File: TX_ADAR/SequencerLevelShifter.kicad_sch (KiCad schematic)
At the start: 16 parts, among them SW4 SW_SPDT, SW6 SW_SPST, SW7 SW_SPST, U15 TXB0101DBV, U16 TXB0101DBV, U17 TXB0101DBV, U18 TXB0101DBV

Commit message: Fixed more issues
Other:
- note removed: "For reset pins, have them reset every time power is turned on?"
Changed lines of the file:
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@@
 	(generator_version "10.0")
 	(paper "A4")
-	(text "For reset pins, have them reset \nevery time power is turned on?"
-		(exclude_from_sim no)
-		(at 167.64 106.426 0)
-		(effects
-			(font
-				(size 2.54 2.54)
-			)
-		)
-	)
 	(text "Level Shifters\n3V3 -> 1V8"
 		(exclude_from_sim no)

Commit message: Finished up adding footprints. Removed unnecessary switches for the TxRST and MRST
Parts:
- removed SW6, SW7: SW_SPST, symbol Switch:SW_SPST
- C29, C30, C31, C38, C39, C40, C41, C42: footprint (none) -> Capacitor_SMD:C_0603_1608Metric_Pad1.08x0.95mm_HandSolder
- R4: footprint (none) -> Resistor_SMD:R_0603_1608Metric_Pad0.98x0.95mm_HandSolder
- SW4: footprint (none) -> 100SP1T1B4M2QE:SW_100SP1T1B4M2QE
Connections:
- net MRST Out: now also U18.4 (B)
- net TxRST Out: now also U16.4 (B)
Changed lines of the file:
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@@
 	(wire
 		(pts
-			(xy 237.49 82.55) (xy 237.49 86.36)
+			(xy 237.49 59.69) (xy 237.49 76.2)
 		)
 		(stroke
@@
 	(wire
 		(pts
-			(xy 162.56 82.55) (xy 162.56 86.36)
+			(xy 189.23 69.85) (xy 226.06 69.85)
 		)
 		(stroke
@@
 	(wire
 		(pts
-			(xy 189.23 69.85) (xy 226.06 69.85)
+			(xy 236.22 59.69) (xy 237.49 59.69)
 		)
 		(stroke
@@
 	(wire
 		(pts
-			(xy 236.22 59.69) (xy 237.49 59.69)
+			(xy 161.29 29.21) (xy 186.69 29.21)
+		)
+		(stroke
+			(width 0.254)
+			(type default)
+			(color 46 82 255 1)
+		)
+	)
+	(wire
+		(pts
+			(xy 209.55 45.72) (xy 198.12 45.72)
+		)
+		(stroke
+			(width 0.254)
+			(type default)
+			(color 255 180 68 1)
+		)
+	)
+	(wire
+		(pts
+			(xy 177.8 73.66) (xy 177.8 59.69)
 		)
 		(stroke
@@
 	(wire
 		(pts
-			(xy 161.29 29.21) (xy 186.69 29.21)
+			(xy 186.69 29.21) (xy 198.12 29.21)
 		)
 		(stroke
@@
 	(wire
 		(pts
-			(xy 209.55 45.72) (xy 198.12 45.72)
+			(xy 172.72 45.72) (xy 161.29 45.72)
 		)
 		(stroke
@@
 	(wire
 		(pts
-			(xy 177.8 73.66) (xy 177.8 59.69)
+			(xy 172.72 26.67) (xy 191.77 26.67)
+		)
+		(stroke
+			(width 0.254)
+			(type default)
+			(color 255 180 68 1)
+		)
+	)
+	(wire
+		(pts
+			(xy 138.43 59.69) (xy 138.43 74.93)
 		)
 		(stroke
@@
 	(wire
 		(pts
-			(xy 186.69 29.21) (xy 198.12 29.21)
+			(xy 161.29 41.91) (xy 161.29 45.72)
 		)
 		(stroke
@@
 	(wire
 		(pts
-			(xy 172.72 45.72) (xy 161.29 45.72)
+			(xy 35.56 36.83) (xy 39.37 36.83)
+		)
+		(stroke
+			(width 0)
+			(type default)
+		)
+	)
+	(wire
+		(pts
+			(xy 161.29 29.21) (xy 161.29 34.29)
+		)
+		(stroke
+			(width 0.254)
+			(type default)
+			(color 46 82 255 1)
+		)
+	)
+	(wire
+		(pts
+			(xy 111.76 24.13) (xy 111.76 49.53)
 		)
 		(stroke
@@
 	(wire
 		(pts
-			(xy 237.49 59.69) (xy 237.49 72.39)
-		)
-		(stroke
-			(width 0)
-			(type default)
-		)
-	)
-	(wire
-		(pts
-			(xy 172.72 26.67) (xy 191.77 26.67)
-		)
-		(stroke
-			(width 0.254)
-			(type default)
-			(color 255 180 68 1)
-		)
-	)
-	(wire
-		(pts
-			(xy 138.43 59.69) (xy 138.43 74.93)
-		)
-		(stroke
-			(width 0)
-			(type default)
-		)
-	)
-	(wire
-		(pts
-			(xy 161.29 41.91) (xy 161.29 45.72)
-		)
-		(stroke
-			(width 0.254)
-			(type default)
-			(color 46 82 255 1)
-		)
-	)
-	(wire
-		(pts
-			(xy 35.56 36.83) (xy 39.37 36.83)
-		)
-		(stroke
-			(width 0)
-			(type default)
-		)
-	)
-	(wire
-		(pts
-			(xy 161.29 29.21) (xy 161.29 34.29)
-		)
-		(stroke
-			(width 0.254)
-			(type default)
-			(color 46 82 255 1)
-		)
-	)
-	(wire
-		(pts
-			(xy 111.76 24.13) (xy 111.76 49.53)
-		)
-		(stroke
-			(width 0.254)
-			(type default)
-			(color 255 180 68 1)
-		)
-	)
-	(wire
-		(pts
-			(xy 162.56 59.69) (xy 162.56 72.39)
+			(xy 162.56 59.69) (xy 162.56 76.2)
 		)
 		(stroke
@@
 	(hierarchical_label "TxRST Out"
 		(shape output)
-		(at 162.56 86.36 270)
+		(at 162.56 76.2 270)
 		(effects
 			(font
@@
 	(hierarchical_label "MRST Out"
 		(shape output)
-		(at 237.49 86.36 270)
+		(at 237.49 76.2 270)
 		(effects
 			(font
@@
 			)
 		)
-		(property "Footprint" ""
+		(property "Footprint" "Capacitor_SMD:C_0603_1608Metric_Pad1.08x0.95mm_HandSolder"
 			(at 86.0552 41.91 0)
 			(hide yes)
@@
 			)
 		)
-		(property "Footprint" ""
+		(property "Footprint" "Capacitor_SMD:C_0603_1608Metric_Pad1.08x0.95mm_HandSolder"
 			(at 74.6252 41.91 0)
 			(hide yes)
@@
 			)
 		)
-		(property "Footprint" ""
+		(property "Footprint" "100SP1T1B4M2QE:SW_100SP1T1B4M2QE"
 			(at 30.48 39.37 0)
 			(hide yes)
@@
 			)
 		)
-		(property "Footprint" ""
+		(property "Footprint" "Capacitor_SMD:C_0603_1608Metric_Pad1.08x0.95mm_HandSolder"
 			(at 210.5152 41.91 0)
 			(hide yes)
@@
 				(path "/5bb7bcfe-c6dc-48dd-b109-2cc47fd52212/81ed6aba-4ce9-46a8-9f2a-cfb086f29798"
 					(reference "C42")
-					(unit 1)
-				)
-			)
-		)
-	)
-	(symbol
-		(lib_id "Switch:SW_SPST")
-		(at 237.49 77.47 90)
-		(unit 1)
-		(body_style 1)
-		(exclude_from_sim no)
-		(in_bom yes)
-		(on_board yes)
-		(in_pos_files yes)
-		(dnp no)
-		(fields_autoplaced yes)
-		(property "Reference" "SW7"
-			(at 238.76 76.1999 90)
-			(show_name no)
-			(do_not_autoplace no)
-			(effects
-				(font
-					(size 1.27 1.27)
-				)
-				(justify right)
-			)
-		)
-		(property "Value" "SW_SPST"
-			(at 238.76 78.7399 90)
-			(hide yes)
-			(show_name no)
-			(do_not_autoplace no)
-			(effects
-				(font
-					(size 1.27 1.27)
-				)
-				(justify right)
-			)
-		)
-		(property "Footprint" ""
-			(at 237.49 77.47 0)
-			(hide yes)
-			(show_name no)
-			(do_not_autoplace no)
-			(effects
-				(font
-					(size 1.27 1.27)
-				)
-			)
-		)
-		(property "Datasheet" ""
-			(at 237.49 77.47 0)
-			(hide yes)
-			(show_name no)
-			(do_not_autoplace no)
-			(effects
-				(font
-					(size 1.27 1.27)
-				)
-			)
-		)
-		(property "Description" "Single Pole Single Throw (SPST) switch"
-			(at 237.49 77.47 0)
-			(hide yes)
-			(show_name no)
-			(do_not_autoplace no)
-			(effects
-				(font
-					(size 1.27 1.27)
-				)
-			)
-		)
-		(pin "1"
-		)
-		(pin "2"
-		)
-		(instances
-			(project "TX_ADAR"
-				(path "/5bb7bcfe-c6dc-48dd-b109-2cc47fd52212/81ed6aba-4ce9-46a8-9f2a-cfb086f29798"
-					(reference "SW7")
 					(unit 1)
 				)
@@
 			)
 		)
-		(property "Footprint" ""
+		(property "Footprint" "Capacitor_SMD:C_0603_1608Metric_Pad1.08x0.95mm_HandSolder"
 			(at 134.3152 41.91 0)
 			(hide yes)
@@
 			)
 		)
-		(property "Footprint" ""
+		(property "Footprint" "Capacitor_SMD:C_0603_1608Metric_Pad1.08x0.95mm_HandSolder"
 			(at 122.8852 41.91 0)
 			(hide yes)
@@
 			)
 		)
-		(property "Footprint" ""
+		(property "Footprint" "Capacitor_SMD:C_0603_1608Metric_Pad1.08x0.95mm_HandSolder"
 			(at 199.0852 41.91 0)
 			(hide yes)
@@
 			)
 		)
-		(property "Footprint" ""
+		(property "Footprint" "Capacitor_SMD:C_0603_1608Metric_Pad1.08x0.95mm_HandSolder"
 			(at 162.2552 41.91 0)
 			(hide yes)
@@
 				(path "/5bb7bcfe-c6dc-48dd-b109-2cc47fd52212/81ed6aba-4ce9-46a8-9f2a-cfb086f29798"
 					(reference "C39")
-					(unit 1)
-				)
-			)
-		)
-	)
-	(symbol
-		(lib_id "Switch:SW_SPST")
-		(at 162.56 77.47 90)
-		(unit 1)
-		(body_style 1)
-		(exclude_from_sim no)
-		(in_bom yes)
-		(on_board yes)
-		(in_pos_files yes)
-		(dnp no)
-		(fields_autoplaced yes)
-		(property "Reference" "SW6"
-			(at 163.83 76.1999 90)
-			(show_name no)
-			(do_not_autoplace no)
-			(effects
-				(font
-					(size 1.27 1.27)
-				)
-				(justify right)
-			)
-		)
-		(property "Value" "SW_SPST"
-			(at 163.83 78.7399 90)
-			(hide yes)
-			(show_name no)
-			(do_not_autoplace no)
-			(effects
-				(font
-					(size 1.27 1.27)
-				)
-				(justify right)
-			)
-		)
-		(property "Footprint" ""
-			(at 162.56 77.47 0)
-			(hide yes)
-			(show_name no)
-			(do_not_autoplace no)
-			(effects
-				(font
-					(size 1.27 1.27)
-				)
-			)
-		)
-		(property "Datasheet" ""
-			(at 162.56 77.47 0)
-			(hide yes)
-			(show_name no)
-			(do_not_autoplace no)
-			(effects
-				(font
-					(size 1.27 1.27)
-				)
-			)
-		)
-		(property "Description" "Single Pole Single Throw (SPST) switch"
-			(at 162.56 77.47 0)
-			(hide yes)
-			(show_name no)
-			(do_not_autoplace no)
-			(effects
-				(font
-					(size 1.27 1.27)
-				)
-			)
-		)
-		(pin "1"
-		)
-		(pin "2"
-		)
-		(instances
-			(project "TX_ADAR"
-				(path "/5bb7bcfe-c6dc-48dd-b109-2cc47fd52212/81ed6aba-4ce9-46a8-9f2a-cfb086f29798"
-					(reference "SW6")
 					(unit 1)
 				)
@@
 			)
 		)
-		(property "Footprint" ""
+		(property "Footprint" "Capacitor_SMD:C_0603_1608Metric_Pad1.08x0.95mm_HandSolder"
 			(at 173.6852 41.91 0)
 			(hide yes)
@@
 			)
 		)
-		(property "Footprint" ""
+		(property "Footprint" "Resistor_SMD:R_0603_1608Metric_Pad0.98x0.95mm_HandSolder"
 			(at 39.37 31.75 0)
 			(hide yes)

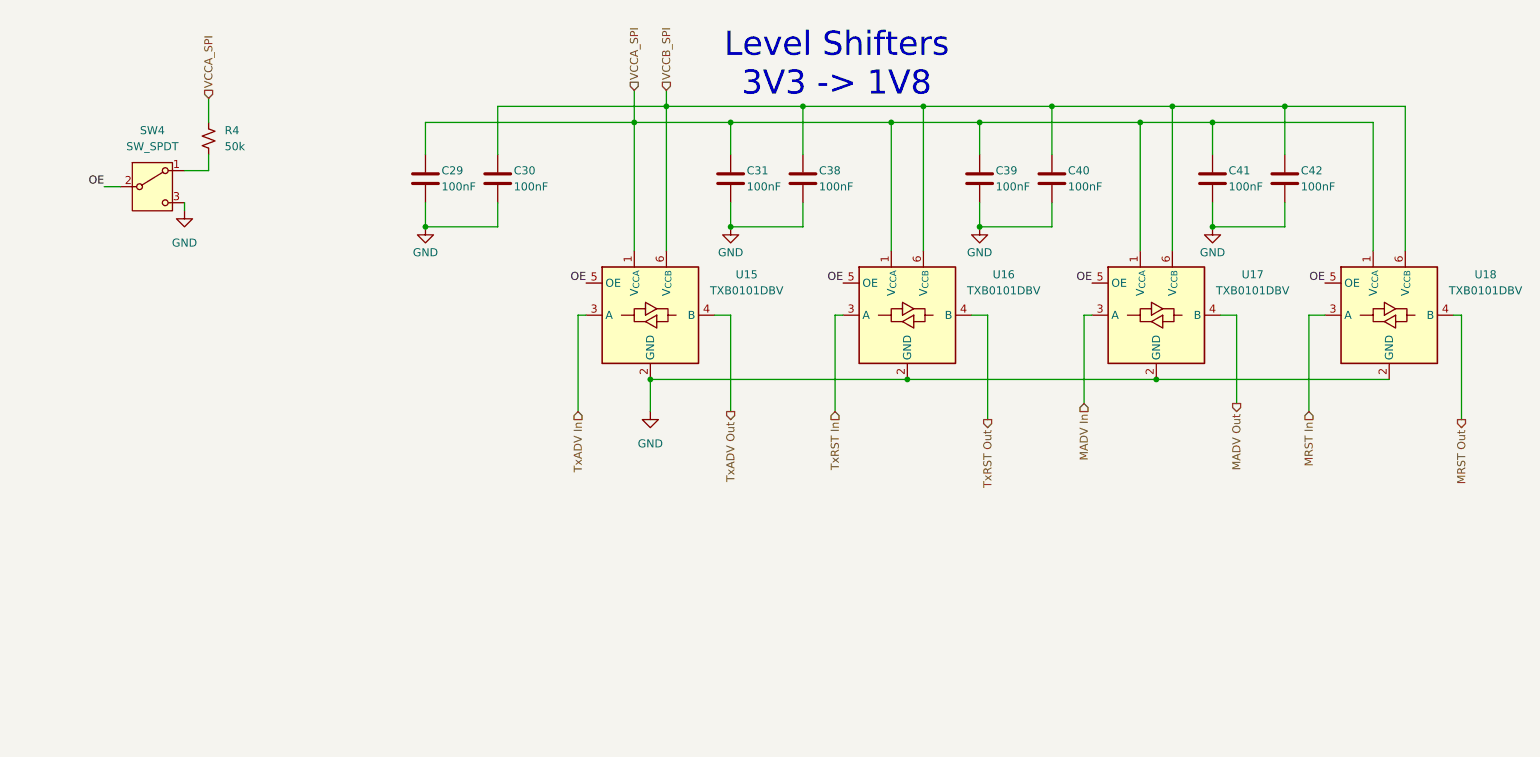
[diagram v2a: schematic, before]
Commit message: Progress on layout
Rough idea of where each component will be relative to each other.
Had some ideas about a component that might be redundant.
Need to determine the final orientation of the components and size of pcb.
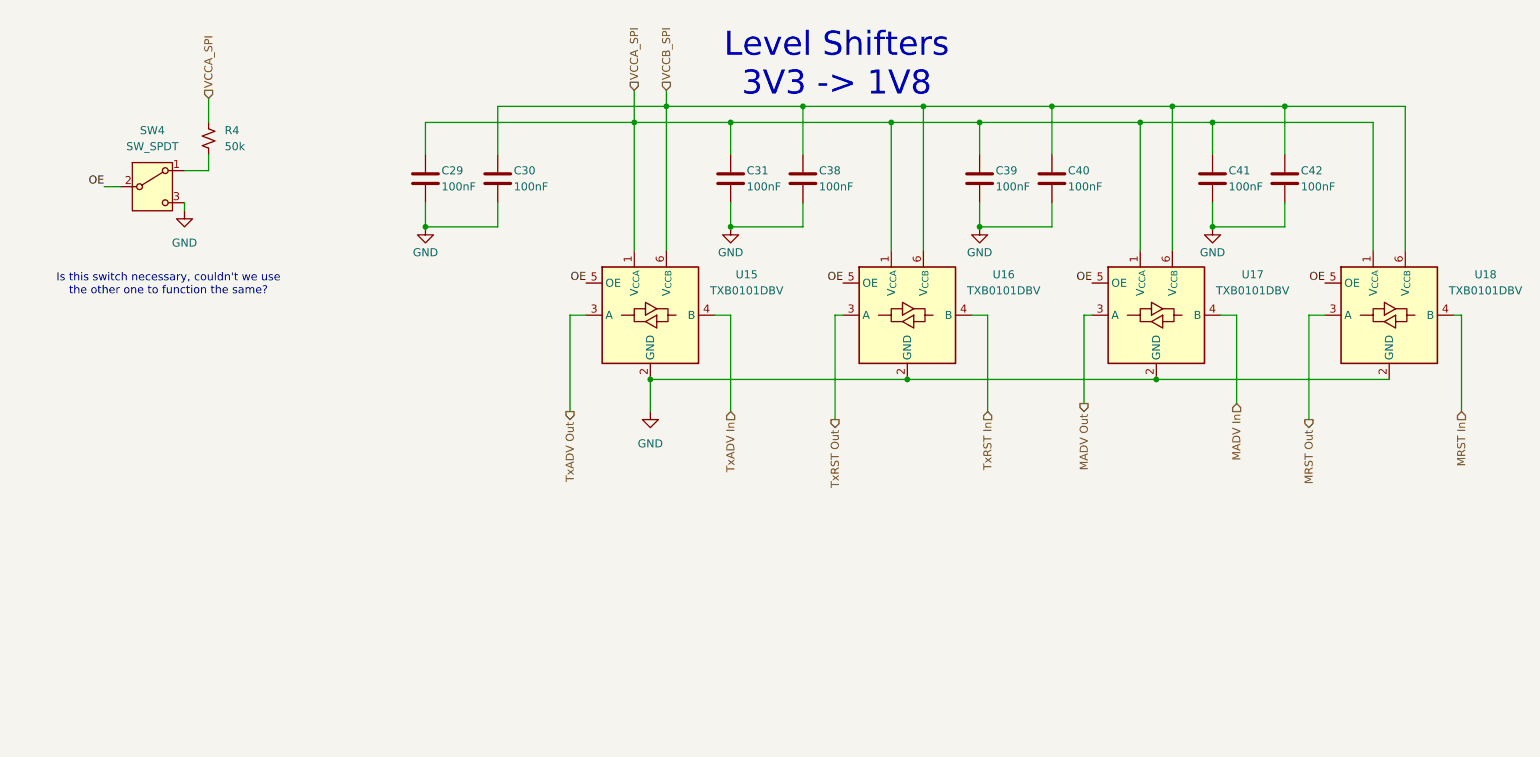
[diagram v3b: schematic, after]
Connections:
- net MADV In: now also U17.4 (B); no longer U17.3 (A)
- net MADV Out: now also U17.3 (A); no longer U17.4 (B)
- net MRST In: now also U18.4 (B); no longer U18.3 (A)
- net MRST Out: now also U18.3 (A); no longer U18.4 (B)
- net TxADV In: now also U15.4 (B); no longer U15.3 (A)
- net TxADV Out: now also U15.3 (A); no longer U15.4 (B)
- net TxRST In: now also U16.4 (B); no longer U16.3 (A)
- net TxRST Out: now also U16.3 (A); no longer U16.4 (B)
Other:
- note added: "Is this switch necessary, couldn't we use the other one to function the same?"
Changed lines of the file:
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@@
+		)
+	)
+	(text "Is this switch necessary, couldn't we use \nthe other one to function the same?"
+		(exclude_from_sim no)
+		(at 33.02 54.864 0)
+		(effects
+			(font
+				(size 1.27 1.27)
+			)
 		)
 	)
@@
 	(wire
 		(pts
+			(xy 96.52 59.69) (xy 96.52 74.93)
+		)
+		(stroke
+			(width 0)
+			(type default)
+		)
+	)
+	(wire
+		(pts
 			(xy 111.76 26.67) (xy 133.35 26.67)
 		)
@@
 	(wire
 		(pts
-			(xy 213.36 74.93) (xy 213.36 59.69)
+			(xy 121.92 74.93) (xy 121.92 59.69)
 		)
 		(stroke
@@
 	(wire
 		(pts
+			(xy 201.93 73.66) (xy 201.93 59.69)
+		)
+		(stroke
+			(width 0)
+			(type default)
+		)
+	)
+	(wire
+		(pts
 			(xy 121.92 29.21) (xy 147.32 29.21)
 		)
@@
 	(wire
 		(pts
+			(xy 177.8 59.69) (xy 177.8 73.66)
+		)
+		(stroke
+			(width 0)
+			(type default)
+		)
+	)
+	(wire
+		(pts
 			(xy 213.36 59.69) (xy 215.9 59.69)
 		)
@@
 	(wire
 		(pts
-			(xy 201.93 59.69) (xy 201.93 73.66)
-		)
-		(stroke
-			(width 0)
-			(type default)
-		)
-	)
-	(wire
-		(pts
 			(xy 133.35 41.91) (xy 133.35 45.72)
 		)
@@
 	(wire
 		(pts
+			(xy 162.56 59.69) (xy 162.56 74.93)
+		)
+		(stroke
+			(width 0)
+			(type default)
+		)
+	)
+	(wire
+		(pts
 			(xy 191.77 26.67) (xy 209.55 26.67)
 		)
@@
 	(wire
 		(pts
-			(xy 97.79 59.69) (xy 99.06 59.69)
+			(xy 96.52 59.69) (xy 99.06 59.69)
+		)
+		(stroke
+			(width 0)
+			(type default)
+		)
+	)
+	(wire
+		(pts
+			(xy 237.49 74.93) (xy 237.49 59.69)
 		)
 		(stroke
@@
 	(wire
 		(pts
-			(xy 97.79 74.93) (xy 97.79 59.69)
+			(xy 213.36 59.69) (xy 213.36 76.2)
 		)
 		(stroke
@@
 	(wire
 		(pts
+			(xy 138.43 59.69) (xy 138.43 76.2)
+		)
+		(stroke
+			(width 0)
+			(type default)
+		)
+	)
+	(wire
+		(pts
 			(xy 35.56 43.18) (xy 35.56 41.91)
 		)
@@
 	(wire
 		(pts
-			(xy 237.49 59.69) (xy 237.49 76.2)
-		)
-		(stroke
-			(width 0)
-			(type default)
-		)
-	)
-	(wire
-		(pts
 			(xy 73.66 29.21) (xy 73.66 34.29)
 		)
@@
 	(wire
 		(pts
-			(xy 121.92 59.69) (xy 121.92 74.93)
-		)
-		(stroke
-			(width 0)
-			(type default)
-		)
-	)
-	(wire
-		(pts
 			(xy 73.66 41.91) (xy 73.66 45.72)
 		)
@@
 	(wire
 		(pts
-			(xy 177.8 73.66) (xy 177.8 59.69)
-		)
-		(stroke
-			(width 0)
-			(type default)
-		)
-	)
-	(wire
-		(pts
 			(xy 186.69 29.21) (xy 198.12 29.21)
 		)
@@
 	(wire
 		(pts
-			(xy 138.43 59.69) (xy 138.43 74.93)
-		)
-		(stroke
-			(width 0)
-			(type default)
-		)
-	)
-	(wire
-		(pts
 			(xy 161.29 41.91) (xy 161.29 45.72)
 		)
@@
 			(type default)
 			(color 255 180 68 1)
-		)
-	)
-	(wire
-		(pts
-			(xy 162.56 59.69) (xy 162.56 76.2)
-		)
-		(stroke
-			(width 0)
-			(type default)
 		)
 	)
@@
 			)
 			(justify right bottom)
+		)
+	)
+	(hierarchical_label "MADV Out"
+		(shape output)
+		(at 177.8 73.66 270)
+		(effects
+			(font
+				(size 1.27 1.27)
+			)
+			(justify right)
 		)
 	)
@@
 		)
 	)
-	(hierarchical_label "MADV Out"
+	(hierarchical_label "TxRST In"
+		(shape input)
+		(at 162.56 74.93 270)
+		(effects
+			(font
+				(size 1.27 1.27)
+			)
+			(justify right)
+		)
+	)
+	(hierarchical_label "MRST Out"
 		(shape output)
+		(at 213.36 76.2 270)
+		(effects
+			(font
+				(size 1.27 1.27)
+			)
+			(justify right)
+		)
+	)
+	(hierarchical_label "MRST In"
+		(shape input)
+		(at 237.49 74.93 270)
+		(effects
+			(font
+				(size 1.27 1.27)
+			)
+			(justify right)
+		)
+	)
+	(hierarchical_label "MADV In"
+		(shape input)
 		(at 201.93 73.66 270)
-		(effects
-			(font
-				(size 1.27 1.27)
-			)
-			(justify right)
-		)
-	)
-	(hierarchical_label "TxADV Out"
-		(shape output)
-		(at 121.92 74.93 270)
 		(effects
 			(font
@@
 	(hierarchical_label "TxRST Out"
 		(shape output)
-		(at 162.56 76.2 270)
-		(effects
-			(font
-				(size 1.27 1.27)
-			)
-			(justify right)
-		)
-	)
-	(hierarchical_label "TxRST In"
-		(shape input)
-		(at 138.43 74.93 270)
-		(effects
-			(font
-				(size 1.27 1.27)
-			)
-			(justify right)
-		)
-	)
-	(hierarchical_label "MADV In"
-		(shape input)
-		(at 177.8 73.66 270)
-		(effects
-			(font
-				(size 1.27 1.27)
-			)
-			(justify right)
-		)
-	)
-	(hierarchical_label "MRST Out"
-		(shape output)
-		(at 237.49 76.2 270)
+		(at 138.43 76.2 270)
 		(effects
 			(font
@@
 		)
 	)
-	(hierarchical_label "MRST In"
-		(shape input)
-		(at 213.36 74.93 270)
+	(hierarchical_label "TxADV Out"
+		(shape output)
+		(at 96.52 74.93 270)
 		(effects
 			(font
@@
 	(hierarchical_label "TxADV In"
 		(shape input)
-		(at 97.79 74.93 270)
-		(effects
-			(font
+		(at 121.92 74.93 270)
+		(effects
+			(font

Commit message: Layout Updates
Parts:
- removed R4: 50k, Resistor_SMD:R_0603_1608Metric_Pad0.98x0.95mm_HandSolder, symbol Device:R_Small_US
- removed SW4: SW_SPDT, 100SP1T1B4M2QE:SW_100SP1T1B4M2QE, symbol Switch:SW_SPDT
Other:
- note removed: "Is this switch necessary, couldn't we use the other one to function the same?"
